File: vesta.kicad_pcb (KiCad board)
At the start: 4 copper layers, 43 x 61.1 mm, 62 parts, among them J1 Solar Panel, J2 Solar Panel, J3 Conn_ARM_SWD_TagConnect_TC203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, U1 STM32WL55CCU6, U2 BQ24074RGTR, U3 TPS63900DSKR, U4 BME688_C3664478, U6 PE4259-63, X1 Q13FC1350000400, X2 X201632MMB4SI

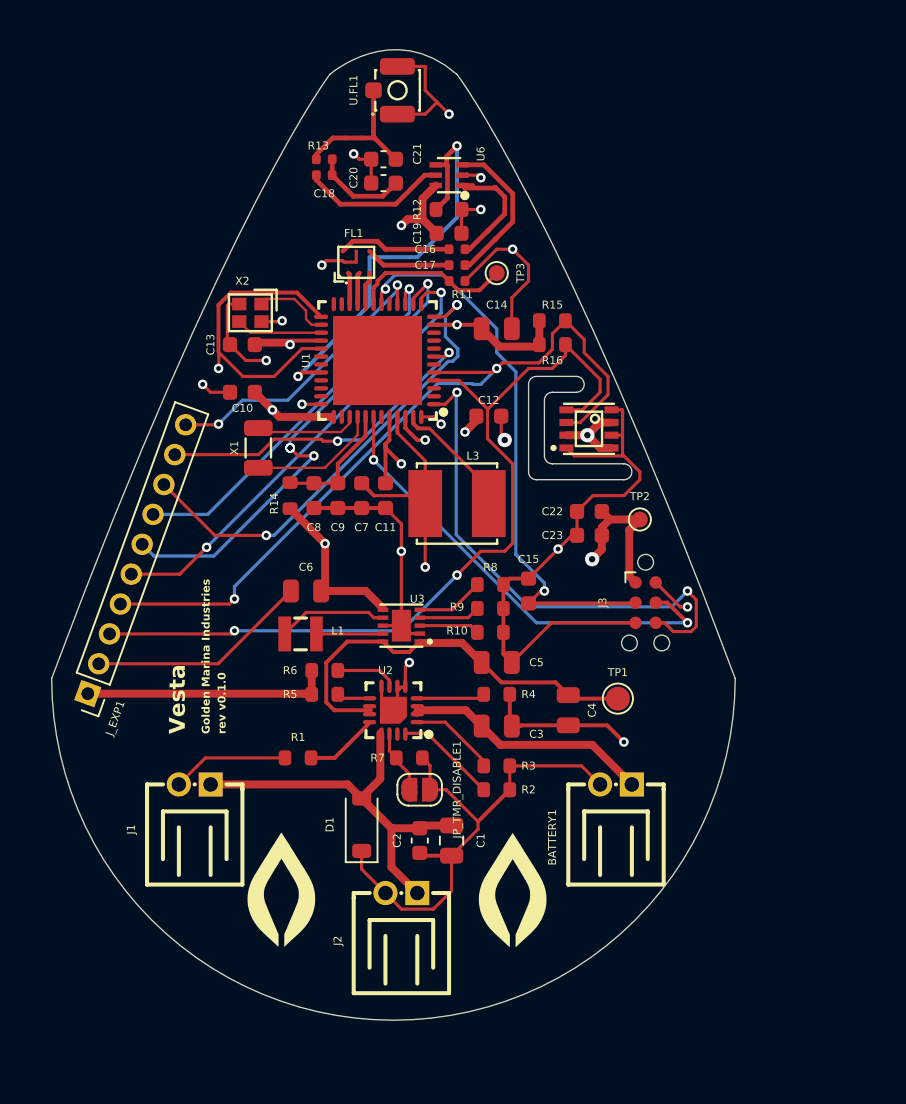
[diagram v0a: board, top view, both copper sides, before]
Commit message: feat: adding the new components into the PCB
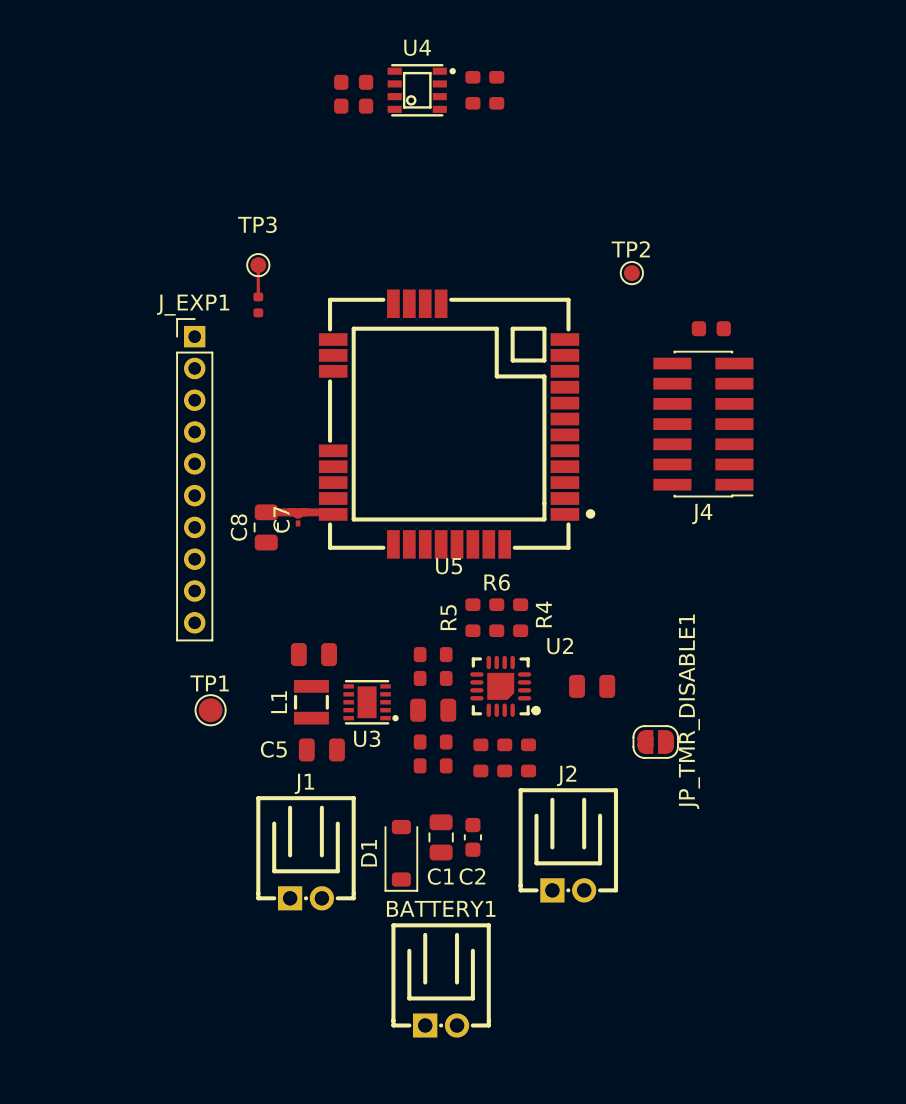
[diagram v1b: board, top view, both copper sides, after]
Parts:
- removed C10, C11, C12, C13, C19: 100nF, PCM_JLCPCB:C_0603
- removed C14: 4.7uF, PCM_JLCPCB:C_0805
- removed C16, C17, C18: 100pF, PCM_JLCPCB:C_0402
- removed C20, C21: DNP, Capacitor_SMD:C_0603_1608Metric
- removed C9: 10nF, PCM_JLCPCB:C_0603
- removed FL1: BALFHB-WL-05D3, JLCImport:BALFHB-WL-05D3
- removed G*** (x2): LOGO, Logo:logo
- removed J3: Conn_ARM_SWD_TagConnect_TC2030-NL, Connector:Tag-Connect_TC2030-IDC-NL_2x03_P1.27mm_Vertical
- removed L3: FNR5040S150MT, JLCImport:FNR5040S150MT
- removed R12: 100kΩ, PCM_JLCPCB:R_0603
- removed R13: 0Ω, PCM_JLCPCB:R_0402
- removed R14: 0kΩ, PCM_JLCPCB:R_0603
- removed U.FL1: Conn_01x03, PCM_JLCPCB:IPEX-SMD_BWIPX-1-001E
- removed U1: STM32WL55CCU6, JLCImport:STM32WL55CCU6
- removed U6: PE4259-63, JLCImport:PE4259-63
- removed X1: Q13FC1350000400, PCM_JLCPCB:FC-135R_L3.2-W1.5
- removed X2: X201632MMB4SI, JLCImport:X201632MMB4SI
- added J4: Conn_02x07_Odd_Even, Connector_PinHeader_1.27mm:PinHeader_2x07_P1.27mm_Vertical_SMD, F.Cu at (59.5, 41.5)
- added U5: RAK3172-T-8-SM-I, JLCImport:RAK3172-T-8-SM-I, F.Cu at (43.5, 41.5)
- C7: value 470nF -> 100nF; footprint PCM_JLCPCB:C_0603 -> Capacitor_SMD:C_01005_0402Metric
- C8: value 1uF -> 4.7uF; footprint PCM_JLCPCB:C_0603 -> Capacitor_SMD:C_0805_2012Metric
- moved C22 30.8 mm to (37.5, 20.0)
- moved C23 30.8 mm to (37.5, 21.5)
- moved TP1 25.6 mm to (28.5, 59.5)
- moved U4 23.9 mm to (41.5, 20.5), turned to 0 degrees
- moved J_EXP1 23.4 mm to (27.5, 36.0), turned to 0 degrees
- moved C15 20.1 mm to (60.0, 35.5), turned to 0 degrees
- moved BATTERY1 18.7 mm to (43.0, 79.3), turned to 0 degrees
- moved R16 16.4 mm to (46.5, 20.5), turned to 90 degrees
- moved TP2 15.5 mm to (55.0, 32.0)
- moved R15 15.3 mm to (45.0, 20.5), turned to 90 degrees
- moved JP_TMR_DISABLE1 15.2 mm to (56.5, 61.5)
- moved TP3 15.0 mm to (31.5, 31.5)
- moved R11 12.6 mm to (31.5, 34.0), turned to 90 degrees
- moved C5 12.3 mm to (35.5, 62.0), turned to 0 degrees
- moved R6 11.3 mm to (46.5, 53.7), turned to -90 degrees
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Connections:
- net /PH3-BOOT0 renamed /MODULE-BOOT0
- C7 pad 1: /SMPS_1V55 -> GND
- C7 pad 2: GND -> /3V3_SYS
- C8 pad 1: /VDDA -> GND
- C8 pad 2: GND -> /3V3_SYS
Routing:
- net GND: track 160.2 -> 0.00 mm, vias 15 -> 0
- net /3V3_SYS: track 76.6 -> 5.35 mm, vias 10 -> 0
- net /I2C1_SCL: track 54.4 -> 0.00 mm, vias 2 -> 0
- net /SMPS_1V55: track 52.9 -> 0.00 mm, vias 2 -> 0
- net /I2C1_SDA: track 49.6 -> 0.00 mm, vias 2 -> 0
- net /NRST: track 35.8 -> 0.00 mm, vias 2 -> 0
- net /SWDIO: track 34.2 -> 0.00 mm, vias 2 -> 0
- net /SWO: track 33.0 -> 0.00 mm, vias 2 -> 0
- net /SPI1_MISO: track 31.0 -> 0.00 mm, vias 6 -> 0
- net /EXP_SPI_CS0: track 30.1 -> 0.00 mm, vias 3 -> 0
- net /SPI1_SCK: track 29.4 -> 0.00 mm, vias 2 -> 0
- net /SWCLK: track 29.2 -> 0.00 mm, vias 2 -> 0
- net /RF_SW_CTRL: track 27.2 -> 0.00 mm, vias 2 -> 0
- net /SYS_RAW: track 26.9 -> 0.00 mm
- net /VIN_SOLAR: track 25.7 -> 0.00 mm
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- removed copper zone on In2.Cu, net /3V3_SYS
- removed copper zone on In1.Cu, net GND
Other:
- board outline removed
- board text removed: "Golden Marina Industries"
- board text removed: "Vesta"
- board text removed: "rev v0.1.0"

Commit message: feat: adding references to all components
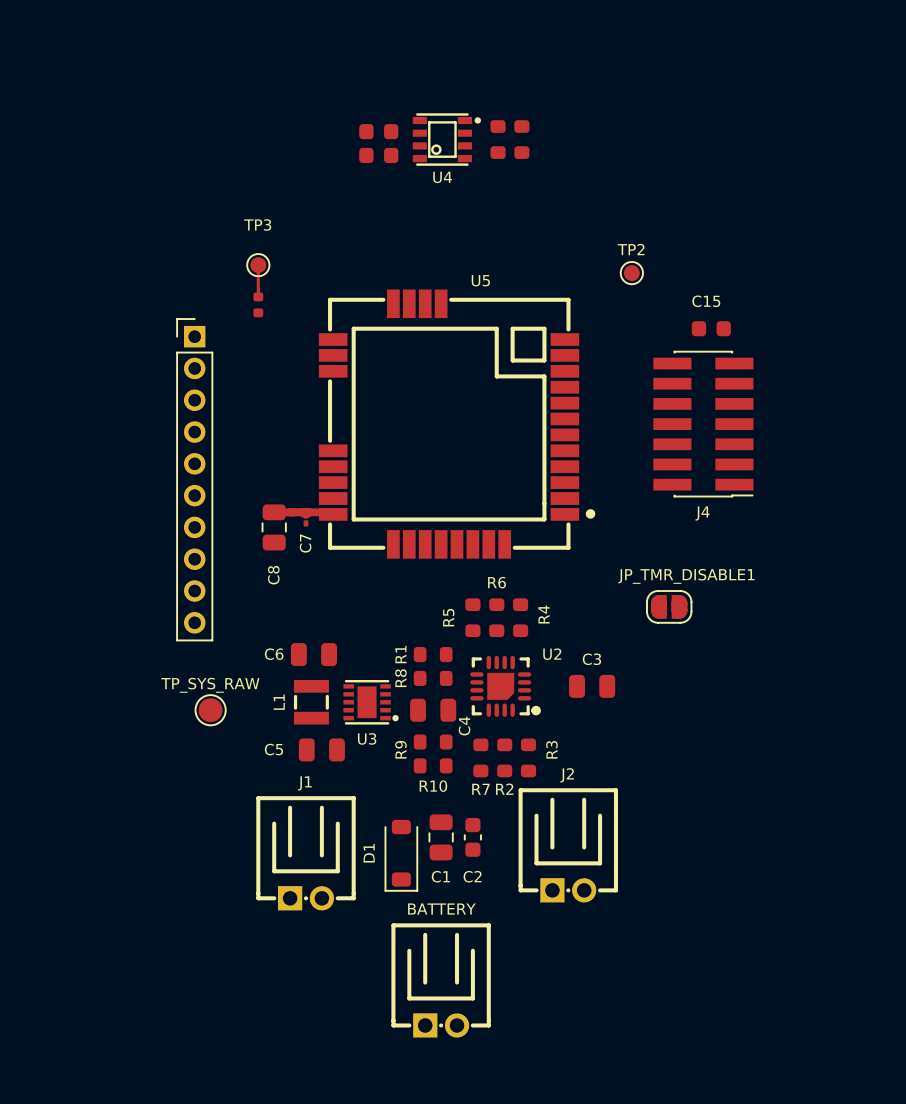
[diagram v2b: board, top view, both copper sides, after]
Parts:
- moved JP_TMR_DISABLE1 8.54 mm to (57.4, 53.0)
- moved C22 3.48 mm to (39.1, 23.1)
- moved C23 3.48 mm to (39.1, 24.6)
- moved R15 3.48 mm to (46.6, 23.6)
- moved R16 3.48 mm to (48.1, 23.6)
- moved U4 3.48 mm to (43.1, 23.6)
- moved C7 0.50 mm to (34.5, 47.5)
- moved C8 0.50 mm to (32.5, 48.0)
- renumbered BATTERY1 to BATTERY, TP1 to TP_SYS_RAW
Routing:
- net /3V3_SYS: track 5.35 -> 4.65 mm
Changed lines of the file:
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@@
 			(effects
 				(font
-					(size 1 1)
+					(size 0.7 0.7)
 					(thickness 0.15)
 				)
@@
 			(effects
 				(font
-					(size 1 1)
+					(size 0.7 0.7)
 					(thickness 0.15)
 				)
@@
 		(tags "capacitor")
 		(property "Reference" "C6"
-			(at 0 -1.68 0)
+			(at -2.5 0 0)
 			(layer "F.SilkS")
-			(hide yes)
 			(effects
 				(font
-					(size 1 1)
+					(size 0.7 0.7)
 					(thickness 0.15)
 				)
@@
 			(at 0 -1.68 0)
 			(layer "F.SilkS")
-			(hide yes)
 			(effects
 				(font
-					(size 1 1)
+					(size 0.7 0.7)
 					(thickness 0.15)
 				)
@@
 	(footprint "Capacitor_SMD:C_01005_0402Metric"
 		(layer "F.Cu")
-		(at 34 47.5 90)
+		(at 34.5 47.5 90)
 		(descr "Capacitor SMD 01005 (0402 Metric), square (rectangular) end terminal, IPC-7351 nominal, (Body size source: http://www.vishay.com/docs/20056/crcw01005e3.pdf)")
 		(tags "capacitor")
 		(property "Reference" "C7"
-			(at 0 -1 90)
+			(at -1.5 0 90)
 			(layer "F.SilkS")
 			(effects
 				(font
-					(size 1 1)
+					(size 0.7 0.7)
 					(thickness 0.15)
 				)
@@
 			(effects
 				(font
-					(size 1 1)
+					(size 0.7 0.7)
 					(thickness 0.15)
 				)
@@
 		(tags "BQ24074RGTR C54313 QFN-16_L3.0-W3.0-P0.50-TL-EP1.7 Texas Instruments")
 		(property "Reference" "U2"
-			(at -3.750189 2.5 0)
+			(at -3.250189 2 0)
 			(layer "F.SilkS")
 			(effects
 				(font
-					(size 1 1)
+					(size 0.7 0.7)
 					(thickness 0.15)
 				)
@@
 	(footprint "PCM_JLCPCB:C_0603"
 		(layer "F.Cu")
-		(at 37.5 20 180)
+		(at 39.080569 23.099949 180)
 		(descr "Capacitor SMD 0603 (1608 Metric), square (rectangular) end terminal, IPC_7351 nominal, (Body size source: IPC-SM-782 page 76, https://www.pcb-3d.com/wordpress/wp-content/uploads/ipc-sm-782a_amendment_1_and_2.pdf), generated with kicad-footprint-generator")
 		(tags "capacitor")
@@
 			(effects
 				(font
-					(size 1 1)
+					(size 0.7 0.7)
 					(thickness 0.15)
 				)
@@
 		(tags "capacitor")
 		(property "Reference" "C4"
-			(at 0 -1.68 0)
+			(at 2 1 270)
 			(layer "F.SilkS")
-			(hide yes)
 			(effects
 				(font
-					(size 1 1)
+					(size 0.7 0.7)
 					(thickness 0.15)
 				)
@@
 		(tags "resistor")
 		(property "Reference" "R1"
-			(at 0 -1.3 0)
+			(at -2 0 90)
 			(layer "F.SilkS")
-			(hide yes)
 			(effects
 				(font
-					(size 1 1)
+					(size 0.7 0.7)
 					(thickness 0.15)
 				)
@@
 	(footprint "Capacitor_SMD:C_0805_2012Metric"
 		(layer "F.Cu")
-		(at 32 48 90)
+		(at 32.5 48 90)
 		(descr "Capacitor SMD 0805 (2012 Metric), square (rectangular) end terminal, IPC-7351 nominal, (Body size source: IPC-SM-782 page 76, https://www.pcb-3d.com/wordpress/wp-content/uploads/ipc-sm-782a_amendment_1_and_2.pdf, https://docs.google.com/spreadsheets/d/1BsfQQcO9C6DZCsRaXUlFlo91Tg2WpOkGARC1WS5S8t0/edit?usp=sharing)")
 		(tags "capacitor")
 		(property "Reference" "C8"
-			(at 0 -1.68 90)
+			(at -3 0 90)
 			(layer "F.SilkS")
 			(effects
 				(font
-					(size 1 1)
+					(size 0.7 0.7)
 					(thickness 0.15)
 				)
@@
 			(at -0.3 -1.7 0)
 			(layer "F.SilkS")
-			(hide yes)
 			(effects
 				(font
-					(size 1 1)
+					(size 0.7 0.7)
 					(thickness 0.15)
 				)
@@
 	(footprint "Jumper:SolderJumper-2_P1.3mm_Open_RoundedPad1.0x1.5mm"
 		(layer "F.Cu")
-		(at 56.5 61.5)
+		(at 57.35 53)
 		(descr "SMD Solder Jumper, 1x1.5mm, rounded Pads, 0.3mm gap, open")
 		(tags "solder jumper open")
 		(property "Reference" "JP_TMR_DISABLE1"
-			(at 2 -2 90)
+			(at 1.15 -2 180)
 			(layer "F.SilkS")
 			(effects
 				(font
-					(size 1 1)
+					(size 0.7 0.7)
 					(thickness 0.15)
 				)
@@
 			(at 0 -2.11 0)
 			(layer "F.SilkS")
+			(hide yes)
 			(effects
 				(font
@@
 			(at 0 -1.3 0)
 			(layer "F.SilkS")
-			(hide yes)
 			(effects
 				(font
-					(size 1 1)
+					(size 0.7 0.7)
 					(thickness 0.15)
 				)
@@
 		(descr "SMD pad as test Point, diameter 1.5mm")
 		(tags "test point SMD pad")
-		(property "Reference" "TP1"
+		(property "Reference" "TP_SYS_RAW"
 			(at 0 -1.648 0)
 			(layer "F.SilkS")
 			(effects
 				(font
-					(size 1 1)
+					(size 0.7 0.7)
 					(thickness 0.15)
 				)
@@
 	(footprint "JLCImport:BME688_C3664478"
 		(layer "F.Cu")
-		(at 41.5 20.5)
+		(at 43.080569 23.599949)
 		(descr "-40℃~+85℃ 0%RH~100%RH 1.71V~3.6V 2.1uA I2C、SPI ±0.5℃ ±3%RH SMD-8P Temperature and Humidity Sensor ROHS")
 		(tags "BME688 Bosch Sensortec C3664478 LGA-8_L3.0-W3.0-P0.80_BME688")
 		(property "Reference" "U4"
-			(at 0 -2.644399 0)
+			(at 0 2.400051 0)
 			(layer "F.SilkS")
 			(effects
 				(font
-					(size 1 1)
+					(size 0.7 0.7)
 					(thickness 0.15)
 				)
@@
 			(effects
 				(font
-					(size 1 1)
+					(size 0.7 0.7)
 					(thickness 0.15)
 				)
@@
 		(tags "resistor")
 		(property "Reference" "R7"
-			(at 0 -1.3 90)
+			(at 2 0 180)
 			(layer "F.SilkS")
-			(hide yes)
 			(effects
 				(font
-					(size 1 1)
+					(size 0.7 0.7)
 					(thickness 0.15)
 				)
@@
 			(effects
 				(font
-					(size 1 1)
+					(size 0.7 0.7)
 					(thickness 0.15)
 				)
@@
 			(effects
 				(font
-					(size 1 1)
+					(size 0.7 0.7)
 					(thickness 0.15)
 				)
@@
 		(tags "resistor")
 		(property "Reference" "R9"
-			(at 0 -1.3 0)
+			(at 2 -0.5 90)
 			(layer "F.SilkS")
-			(hide yes)
 			(effects
 				(font
-					(size 1 1)
+					(size 0.7 0.7)
 					(thickness 0.15)
 				)
@@
 			(effects
 				(font
-					(size 1 1)
+					(size 0.7 0.7)
 					(thickness 0.15)
 				)
@@
 			(effects
 				(font
-					(size 1 1)
+					(size 0.7 0.7)
 					(thickness 0.15)
 				)
@@
 			(effects
 				(font
-					(size 1 1)
+					(size 0.7 0.7)
 					(thickness 0.15)
 				)
@@
 	(footprint "PCM_JLCPCB:C_0603"
 		(layer "F.Cu")
-		(at 37.5 21.5 180)
+		(at 39.080569 24.599949 180)
 		(descr "Capacitor SMD 0603 (1608 Metric), square (rectangular) end terminal, IPC_7351 nominal, (Body size source: IPC-SM-782 page 76, https://www.pcb-3d.com/wordpress/wp-content/uploads/ipc-sm-782a_amendment_1_and_2.pdf), generated with kicad-footprint-generator")
 		(tags "capacitor")
@@
 	(footprint "PCM_JLCPCB:R_0603"
 		(layer "F.Cu")
-		(at 46.5 20.5 90)
+		(at 48.080569 23.599949 90)
 		(descr "Resistor SMD 0603 (1608 Metric), square (rectangular) end terminal, IPC_7351 nominal, (Body size source: IPC-SM-782 page 72, https://www.pcb-3d.com/wordpress/wp-content/uploads/ipc-sm-782a_amendment_1_and_2.pdf), generated with kicad-footprint-generator")
 		(tags "resistor")
@@
 			(effects
 				(font
-					(size 1 1)
+					(size 0.7 0.7)
 					(thickness 0.15)
 				)
@@
 			(effects
 				(font
-					(size 1 1)
+					(size 0.7 0.7)
 					(thickness 0.15)
 				)
@@
 		(descr "-25℃~+85℃ 1 1x2P 2 250V 2A 2P 2mm 4.7mm 6.05mm 6mm Brass PA66 PH Right Angle Tin UL94V-0 White 弯插,P=2mm Wire To Board Connector ROHS")
 		(tags "C5359610 CONN-TH_2P-P2.00_GP01-2001WR-2P WAFER-PH2.0-2PWZ XUNPU")
-		(property "Reference" "BATTERY1"
+		(property "Reference" "BATTERY"
 			(at 0 -7.299949 0)
 			(layer "F.SilkS")
 			(effects
 				(font
-					(size 1 1)
+					(size 0.7 0.7)
 					(thickness 0.15)
 				)
@@
 			(effects
 				(font
-					(size 1 1)
+					(size 0.7 0.7)
 					(thickness 0.15)
 				)
@@
 		(tags "resistor")
 		(property "Reference" "R8"
-			(at 0 -1.3 0)
+			(at 2 0 90)
 			(layer "F.SilkS")
-			(hide yes)
 			(effects
 				(font
-					(size 1 1)
+					(size 0.7 0.7)
 					(thickness 0.15)
 				)
@@
 		(tags "resistor")
 		(property "Reference" "R2"
-			(at 0 -1.3 90)
+			(at -2 0 180)
 			(layer "F.SilkS")
-			(hide yes)
 			(effects
 				(font
-					(size 1 1)
+					(size 0.7 0.7)
 					(thickness 0.15)
 				)
@@
 			(effects
 				(font
-					(size 1 1)
+					(size 0.7 0.7)
 					(thickness 0.15)
 				)
@@
 		(tags "resistor")
 		(property "Reference" "R3"
-			(at 0 -1.3 90)
+			(at 0.5 1.5 90)
 			(layer "F.SilkS")
-			(hide yes)
 			(effects
 				(font
-					(size 1 1)
+					(size 0.7 0.7)
 					(thickness 0.15)
 				)
@@
 		(tags "C19723908 RAK3172-T-8-SM-I RAKwireless WIRELM-SMD_32P-L15.5-W15.0-P1.00")
 		(property "Reference" "U5"
-			(at 0 -8.96874 0)
+			(at -2 9 0)
 			(layer "F.SilkS")
 			(effects
 				(font
-					(size 1 1)
+					(size 0.7 0.7)
 					(thickness 0.15)
 				)
@@
 	(footprint "PCM_JLCPCB:R_0603"
 		(layer "F.Cu")
-		(at 45 20.5 90)
+		(at 46.580569 23.599949 90)
 		(descr "Resistor SMD 0603 (1608 Metric), square (rectangular) end terminal, IPC_7351 nominal, (Body size source: IPC-SM-782 page 72, https://www.pcb-3d.com/wordpress/wp-content/uploads/ipc-sm-782a_amendment_1_and_2.pdf), generated with kicad-footprint-generator")
 		(tags "resistor")
@@
 	)
 	(segment
-		(start 33.5 47.05)
-		(end 32 47.05)
-		(width 0.5)
-		(layer "F.Cu")
-		(net "/3V3_SYS")
-	)
-	(segment
 		(start 36.212613 47.18)
 		(end 36.082613 47.05)
@@
 	)
 	(segment
-		(start 34.2 47.05)
-		(end 34.1 47.15)
+		(start 34.7 47.05)
+		(end 34.6 47.15)
 		(width 0.5)
 		(layer "F.Cu")
@@
 	)
 	(segment
-		(start 33.9 47.15)
-		(end 33.8 47.05)
+		(start 34.4 47.15)
+		(end 34.3 47.05)
 		(width 0.5)
 		(layer "F.Cu")
@@
 	)
 	(segment
-		(start 34.1 47.15)
-		(end 33.9 47.15)
+		(start 33.5 47.05)
+		(end 32.5 47.05)
 		(width 0.5)
 		(layer "F.Cu")

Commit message: feat: small footprint fixes before starting the routing
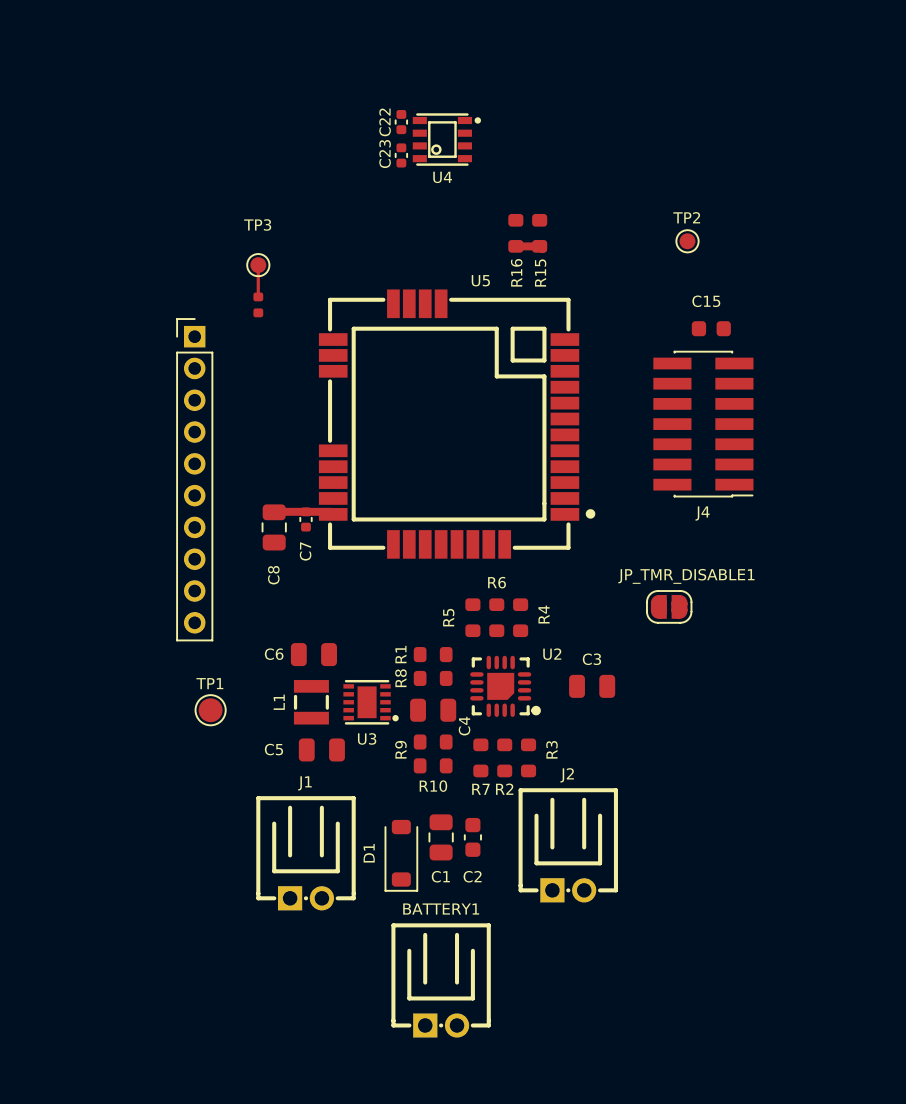
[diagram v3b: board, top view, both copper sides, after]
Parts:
- C22, C23: footprint PCM_JLCPCB:C_0603 -> Capacitor_SMD:C_0402_1005Metric
- C7: footprint Capacitor_SMD:C_01005_0402Metric -> Capacitor_SMD:C_0402_1005Metric
- moved R15 6.46 mm to (49.2, 29.5), turned to -90 degrees
- moved R16 5.91 mm to (47.7, 29.5), turned to -90 degrees
- moved TP2 4.03 mm to (58.5, 30.0)
- moved C22 1.54 mm to (40.5, 22.5), turned to -90 degrees
- moved C23 1.42 mm to (40.5, 24.6), turned to -90 degrees
- renumbered BATTERY to BATTERY1, TP_SYS_RAW to TP1
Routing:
- net /3V3_SYS: track 4.65 -> 5.55 mm
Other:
- copper layers 4 -> 2
